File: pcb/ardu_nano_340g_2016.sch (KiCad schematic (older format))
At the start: 37 parts, among them J1 USB_B_Mini, J2 Conn_01x15, J3 Conn_01x15, J4 Conn_02x03_Odd_Even, U1 CH340G-JEC, U2 ATMEGA328P-AU, U3 LM1117-5.0, Y1 16MHz Resonator, Y2 12Mhz Resonator

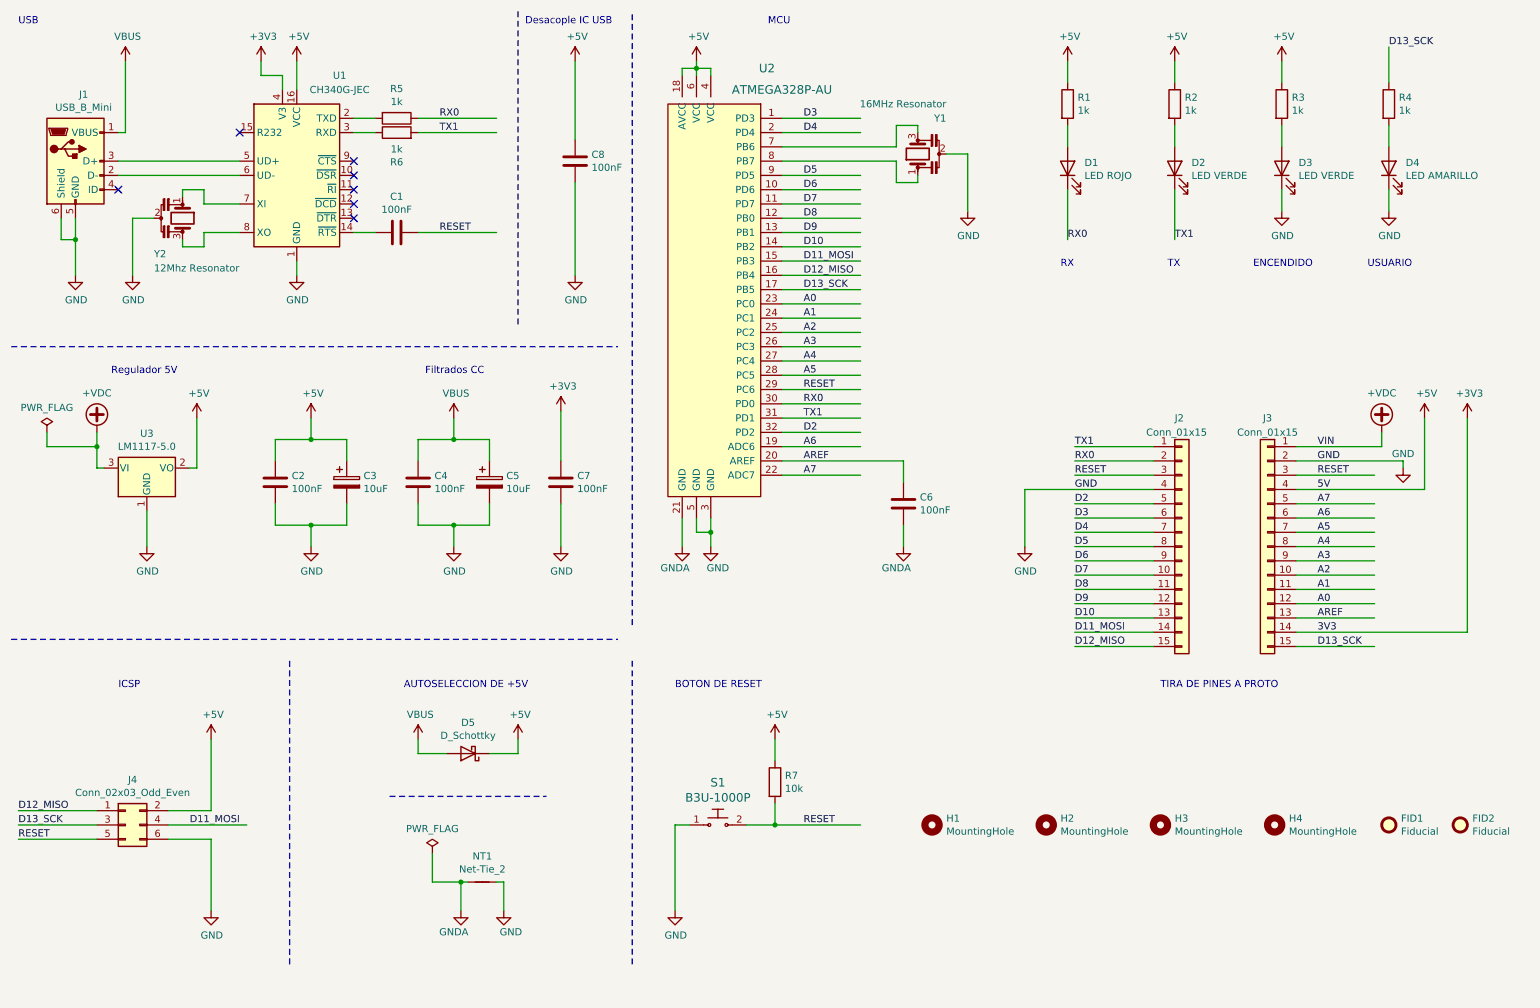
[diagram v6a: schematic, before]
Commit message: V2.3 Se agregó capacitor desacople MCU
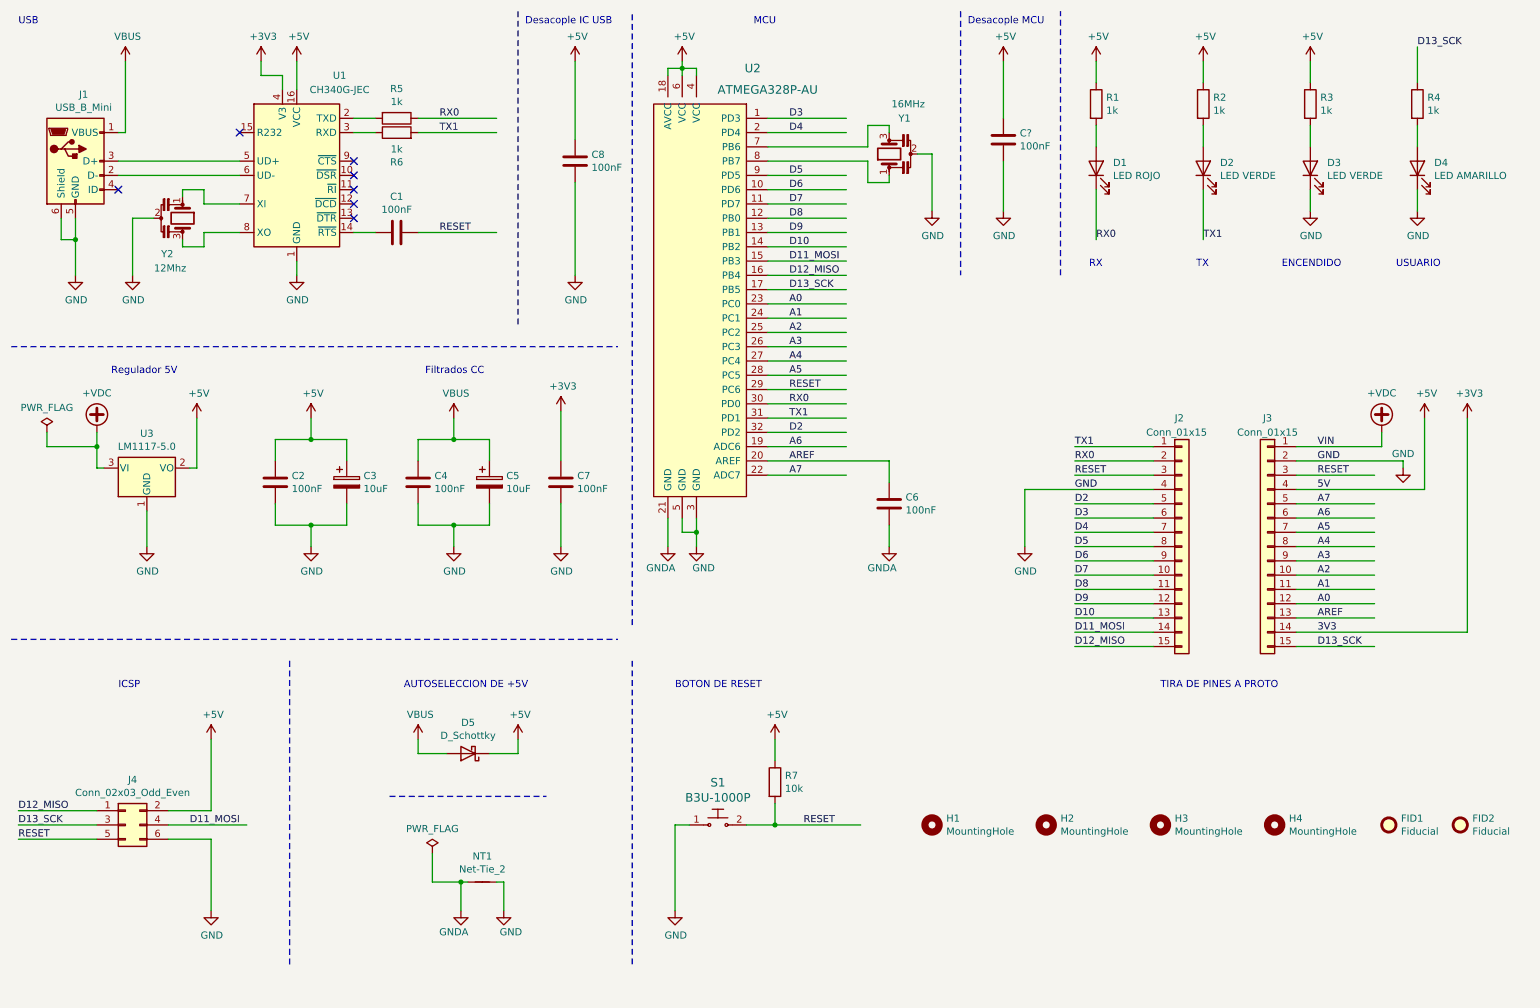
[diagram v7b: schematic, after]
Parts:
- added C?: 100nF, Capacitor_SMD:C_0805_2012Metric_Pad1.18x1.45mm_HandSolder, symbol Device:C
- Y1: value 16MHz Resonator -> 16MHz
- Y2: value 12Mhz Resonator -> 12Mhz
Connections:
- wire segments 179 -> 181
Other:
- note added: "Desacople MCU"
- moved on the sheet: C6, D1, D2, D3, D4, R1, R2, R3, R4, U2, Y1

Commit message: avances del 17/10/2020
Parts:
- gave numbers to parts that had none: 1
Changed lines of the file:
@@
 Sheet 1 1
 Title "ardu_nano_340g_2016"
-Date "2020-10-14"
-Rev "3.1"
+Date "2020-10-18"
+Rev "2.3"
 Comp "Autor: Juan Esteban Carrique <jecarrique@sinc.unl.edu.ar>"
 Comment1 "Revisor par: Alejandro Gorrin"
 Comment2 "Revisor Docente: Diego Brengi"
 Comment3 "Licencia: CC BY-NC-SA"
-Comment4 "V2.2 Se agregó capacitor desacople IC USB y se redujo huella resonadores"
+Comment4 "V2.3 Se agregó capacitor desacople MCU"
 $EndDescr
 $Comp
@@
 	6650 1700 5950 1700
 $Comp
-L Device:C C?
+L Device:C C9
 U 1 1 5F9409DC
 P 7600 1550
-F 0 "C?" H 7715 1596 50  0000 L CNN
+F 0 "C9" H 7715 1596 50  0000 L CNN
 F 1 "100nF" H 7715 1505 50  0000 L CNN
 F 2 "Capacitor_SMD:C_0805_2012Metric_Pad1.18x1.45mm_HandSolder" H 7638 1400 50  0001 C CNN
@@
 $EndComp
 $Comp
-L power:GND #PWR?
+L power:GND #PWR042
 U 1 1 5F9409E2
 P 7600 2050
-F 0 "#PWR?" H 7600 1800 50  0001 C CNN
+F 0 "#PWR042" H 7600 1800 50  0001 C CNN
 F 1 "GND" H 7605 1877 50  0000 C CNN
 F 2 "" H 7600 2050 50  0001 C CNN
@@
 $EndComp
 $Comp
-L power:+5V #PWR?
+L power:+5V #PWR041
 U 1 1 5F9409E8
 P 7600 1000
-F 0 "#PWR?" H 7600 850 50  0001 C CNN
+F 0 "#PWR041" H 7600 850 50  0001 C CNN
 F 1 "+5V" H 7615 1173 50  0000 C CNN
 F 2 "" H 7600 1000 50  0001 C CNN
